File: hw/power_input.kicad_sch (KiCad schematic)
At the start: 38 parts, among them Q101 SQD50P08-25L, Q102 IPD90N10S4-06, Q103 SQM120P10-10m1L, Q104 SQM120P10-10m1L, U101 TLV3201, U102 UCC27517A

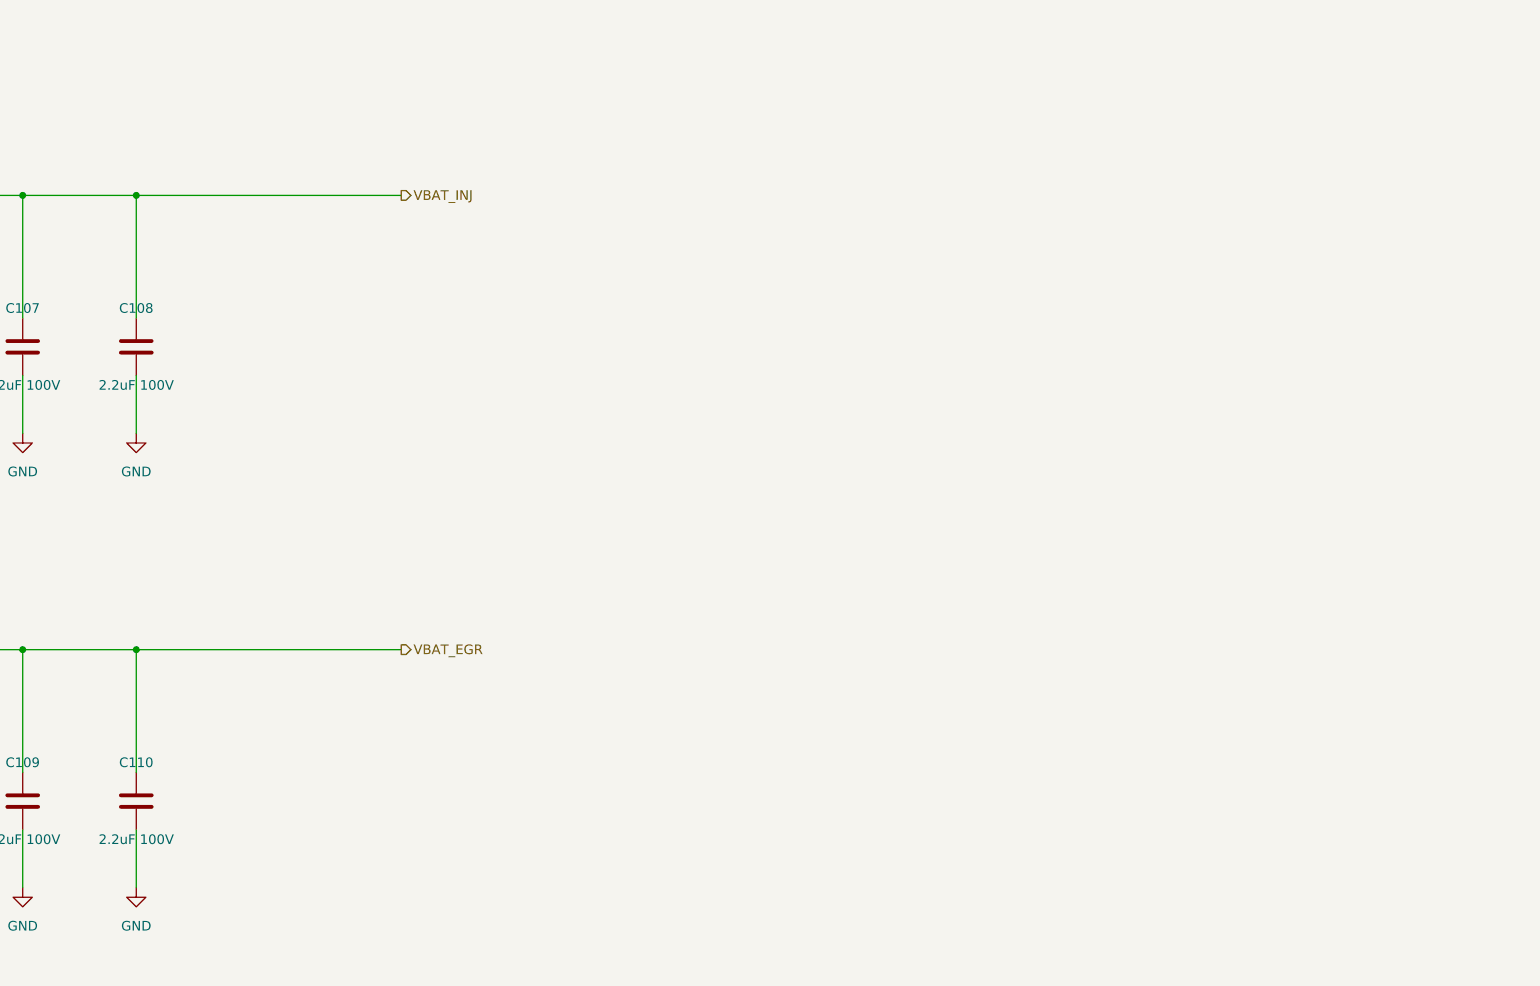
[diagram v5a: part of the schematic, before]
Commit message: Filter the two POWER-PATH feeds: 33-48 dB over CISPR 25 Class 5 without
New block feed_emi.cir measures conducted emissions through a CISPR 25
5 uH / 50 ohm LISN; run_sim scores the hold chopping, boost ripple and
EGR PWM harmonics against the Class 5 limits, band by band. As drawn the
injector feed was 33 dB over and the EGR feed 48 dB over, since
POWER-PATH took both off pin 21's filter.

Each feed now has a Coilcraft XAL1510-103 (10 uH), two 82 uF HXC bulk
cans and two dampers (0.68 ohm + HXC): 17.7 dB (injector) and 9.3 dB
(EGR) under the limit at 25 kHz. The dampers hold the filter's output
impedance to 0.64 ohm aged, 1.47x under the constant-power loads'
-0.94 ohm at 9 V. Pulse 2a puts 48.7 V across the inductor (55 V
rating), and the loads now see 28.7 V instead of 73.3 V.

Firmware requirement: hold chopping and EGR PWM at or below 25 kHz.
Decisions log section 10.
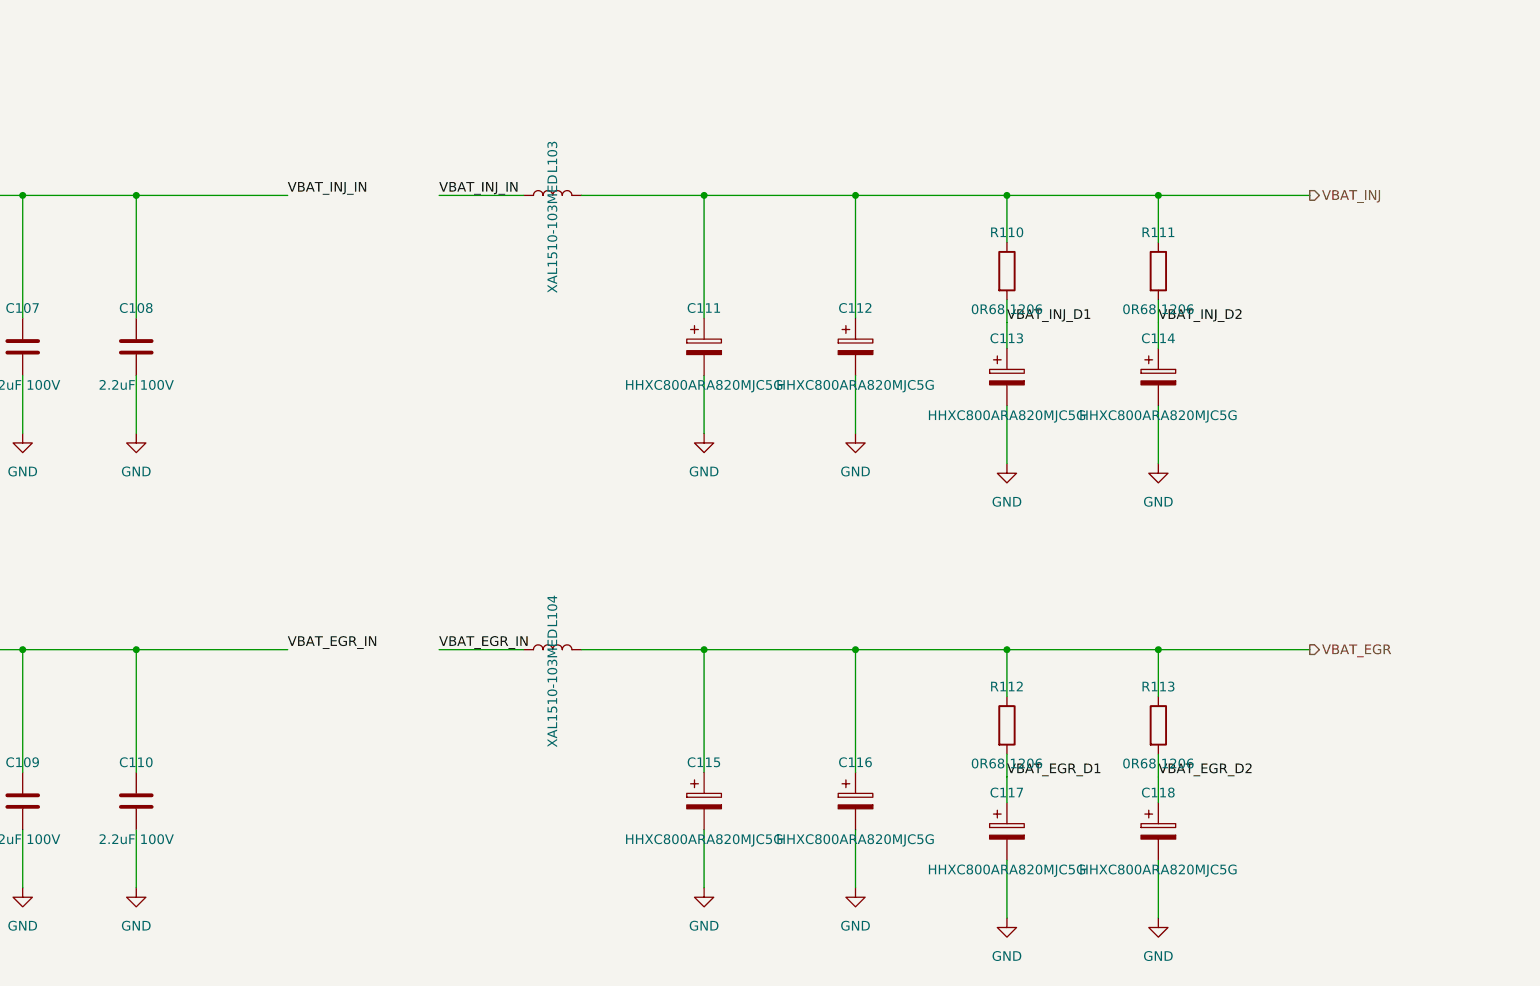
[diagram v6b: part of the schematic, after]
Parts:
- added C111, C112, C113, C114, C115, C116, C117, C118: HHXC800ARA820MJC5G, Capacitor_SMD:CP_Elec_10x12.5, symbol Device:C_Polarized
- added L103, L104: XAL1510-103MED, Inductor_SMD:L_Coilcraft_XAL1510-103, symbol Device:L
- added R110, R111, R112, R113: 0R68 1206, Resistor_SMD:R_1206_3216Metric, symbol Device:R
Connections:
- net GND: now also C111.2, C112.2, C113.2, C114.2, C115.2, C116.2, C117.2, C118.2
- net VBAT_EGR: now also C115.1, C116.1, L104.2, R112.1, R113.1; no longer C109.1, C110.1, D109.1 (K), D110.1 (K), Q104.3 (S)
- net VBAT_INJ: now also C111.1, C112.1, L103.2, R110.1, R111.1; no longer C107.1, C108.1, D106.1 (K), D107.1 (K), Q103.3 (S)
- new net VBAT_EGR_D1: C117.1, R112.2
- new net VBAT_EGR_D2: C118.1, R113.2
- new net VBAT_EGR_IN: C109.1, C110.1, D109.1 (K), D110.1 (K), L104.1, Q104.3 (S)
- new net VBAT_INJ_D1: C113.1, R110.2
- new net VBAT_INJ_D2: C114.1, R111.2
- new net VBAT_INJ_IN: C107.1, C108.1, D106.1 (K), D107.1 (K), L103.1, Q103.3 (S)

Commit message: Stable schematic UUIDs, so regenerating never breaks the board's links; correct the power_input gate-drive note
- schlib and gen_project derive UUIDs (sheet title + reference) instead of uuid4;
  regenerating is byte-identical (test_schlib.py)
- board rebuilt on the new links; check_pcb now fails on any stale footprint path
  (KiCad's parity check matches by reference and misses it)
- power_input: Q1 is passive, Q2 driven by TLV3201 + UCC27517A; the OPEN note was stale
- status: Resume-here rewritten for 15 Oct
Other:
- note added: "GATE DRIVE -- both power-path gates are driven:\n VBAT_REV_GATE Q1 is a P-FET: 47k gate to ground, zener gate-to-source. No controller needed.\n NCLAMP_GATE Q2 (negative clamp): TLV3201-Q1 comparator into a UCC27517A-Q1 driver.\n Engage below -100 mV, release above -5 mV (see neg_clamp_control).\nKeep U102 at Q2's gate with a short return to Q2's source: the clamp's speed is the gate loop's."
- note removed: "OPEN -- two gates on this sheet are intentionally undriven, and ERC will report them:\n VBAT_REV_GATE ideal-diode controller for Q1. No part chosen. Its turn-off time is load-bearing\n (reverse_battery.cir models it with none) but nothing sources that number yet.\n NCLAMP_GATE comparator for Q2, sensing VIN against -0.1 V. No part chosen. Its propagation\n delay is the last unmodelled term in neg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"
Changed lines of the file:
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@@
     (effects (font (size 1.27 1.27)) (justify left))
   )
-  (text "OPEN -- two gates on this sheet are intentionally undriven, and ERC will report them:\\n  VBAT_REV_GATE   ideal-diode controller for Q1. No part chosen. Its turn-off time is load-bearing\\n                  (reverse_battery.cir models it with none) but nothing sources that number yet.\\n  NCLAMP_GATE     comparator for Q2, sensing VIN against -0.1 V. No part chosen. Its propagation\\n                  delay is the last unmodelled term in negative_pulses.cir -- VIN sits at the\\n                  Schottky's -0.53 V for exactly that long before the clamp engages.\\nNeither pinout can be drawn without choosing a part, and this project does not guess parts into copper." (at 30.0 150.0 0)
+  (text "GATE DRIVE -- both power-path gates are driven:\\n  VBAT_REV_GATE   Q1 is a P-FET: 47k gate to ground, zener gate-to-source. No controller needed.\\n  NCLAMP_GATE     Q2 (negative clamp): TLV3201-Q1 comparator into a UCC27517A-Q1 driver.\\n                  Engage below -100 mV, release above -5 mV (see neg_clamp_control).\\nKeep U102 at Q2's gate with a short return to Q2's source: the clamp's speed is the gate loop's." (at 30.0 150.0 0)
     (effects (font (size 1.6 1.6)) (justify left))
   )
